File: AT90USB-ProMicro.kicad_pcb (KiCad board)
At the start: 2 copper layers, 18 x 33 mm, 21 parts, among them J1 Conn_01x12, J2 Conn_01x12, J3 Conn_01x03, U1 AT90USB162-16MU, U2 MCP1703A-3302_SOT23, X1 O925208MEDA4SI

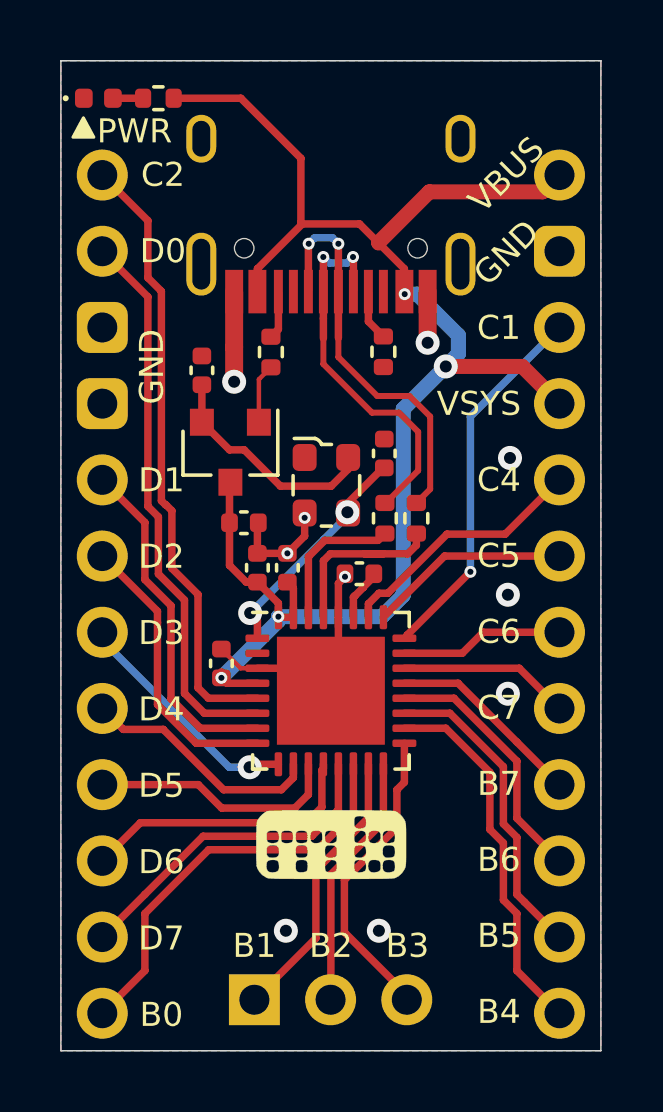
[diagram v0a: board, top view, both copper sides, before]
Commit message: changed oscillator for crystal, 3225 gnd on 2 and 4.
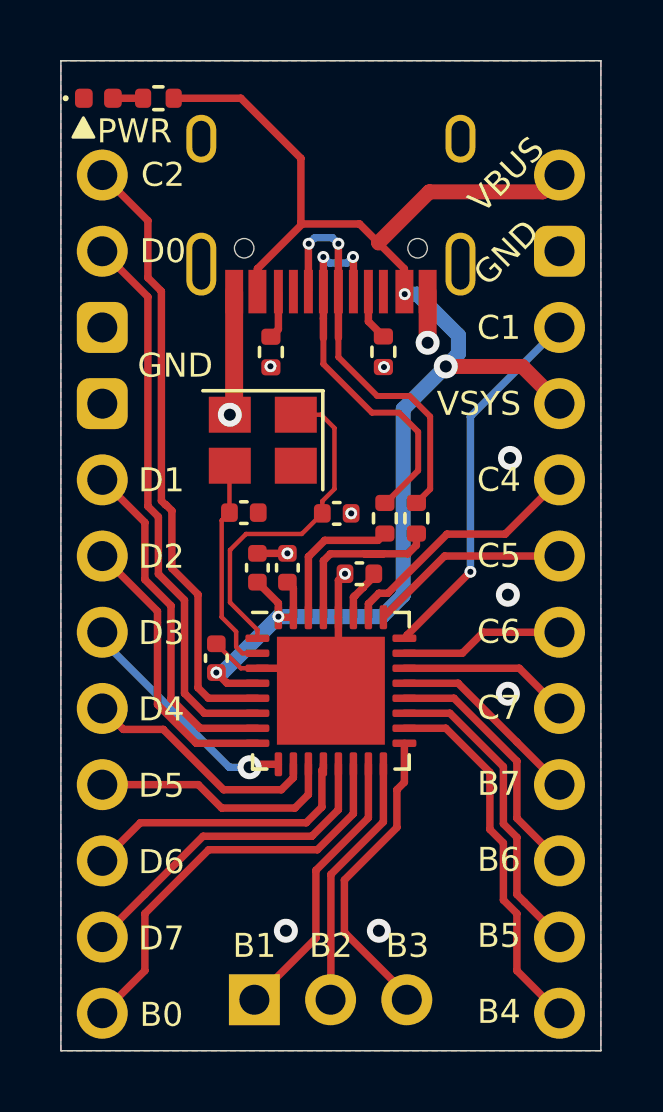
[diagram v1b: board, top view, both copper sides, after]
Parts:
- removed C7: 15pF 0402, Capacitor_SMD:C_0402_1005Metric
- removed Ref**: Val**, MechboardsLogo:mechboardsLOGO_5mm
- removed U2: MCP1703A-3302_SOT23, Package_TO_SOT_SMD:SOT-23
- removed X1: O925208MEDA4SI, Oscillator:Oscillator_SMD_ECS_2520MV-xxx-xx-4Pin_2.5x2.0mm
- added Y1: 8MHz, Crystal:Crystal_SMD_3225-4Pin_3.2x2.5mm, F.Cu at (129.7, 73.6)
- C1, C6: value 0.1uf 0402 -> 0402 22pf
- moved C6 4.94 mm to (129.1, 76.1), turned to 180 degrees
- moved C1 3.11 mm to (132.2, 76.1), turned to 180 degrees
- moved C5 0.24 mm to (128.2, 80.9)
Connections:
- C1 pad 1: VBUS -> GND
- C1 pad 2: GND -> XTAL1
- C6 pad 2: Net-(C6-Pad2) -> XTAL2
- U1 pad 2: (no net) -> XTAL2
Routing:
- net Net-(C6-Pad2): track 7.78 -> 0.00 mm
- net XTAL2: track 0.00 -> 7.25 mm
- net VBUS: track 54.2 -> 50.2 mm
- net XTAL1: track 7.66 -> 11.4 mm, vias 2 -> 0
- net GND: track 18.5 -> 15.4 mm, vias 10 -> 12

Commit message: Added a Kiwi pattern on both sides of the board to make it look "Pretty"
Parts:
- added G***: LOGO, Graphic:tilepattern, F.Cu at (132.0, 77.5)
- added G***: LOGO, Graphic:tilepattern, B.Cu at (132.0, 77.5)
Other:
- board text removed: "PWR"

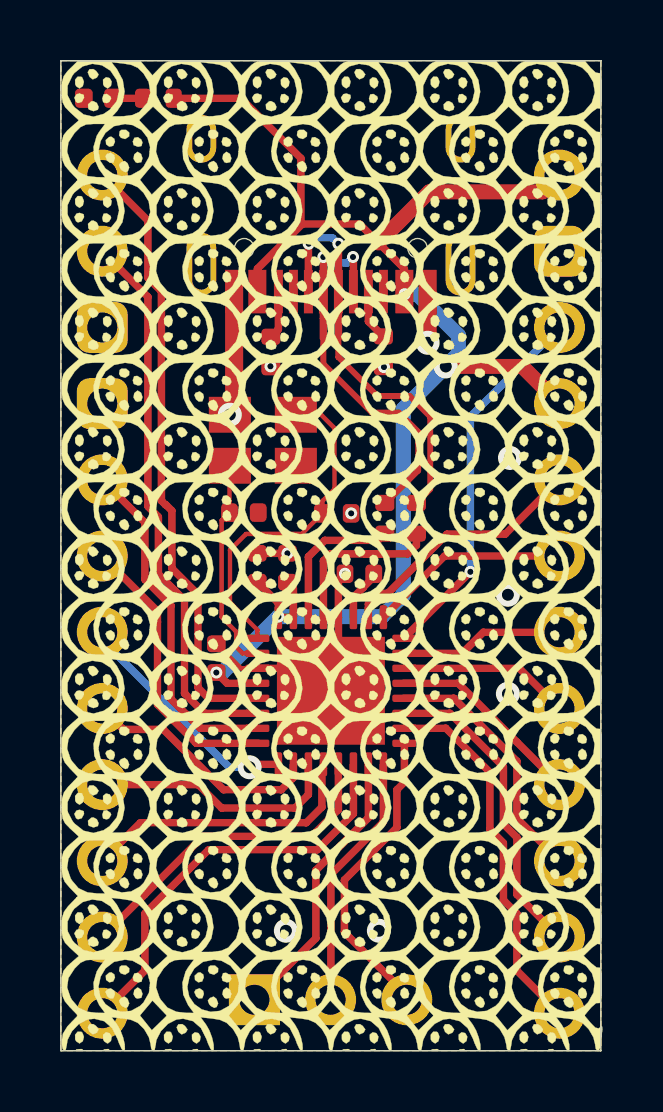
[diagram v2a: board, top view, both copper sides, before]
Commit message: Changed pattern out for a geo graphic looking one, much nicer i think.
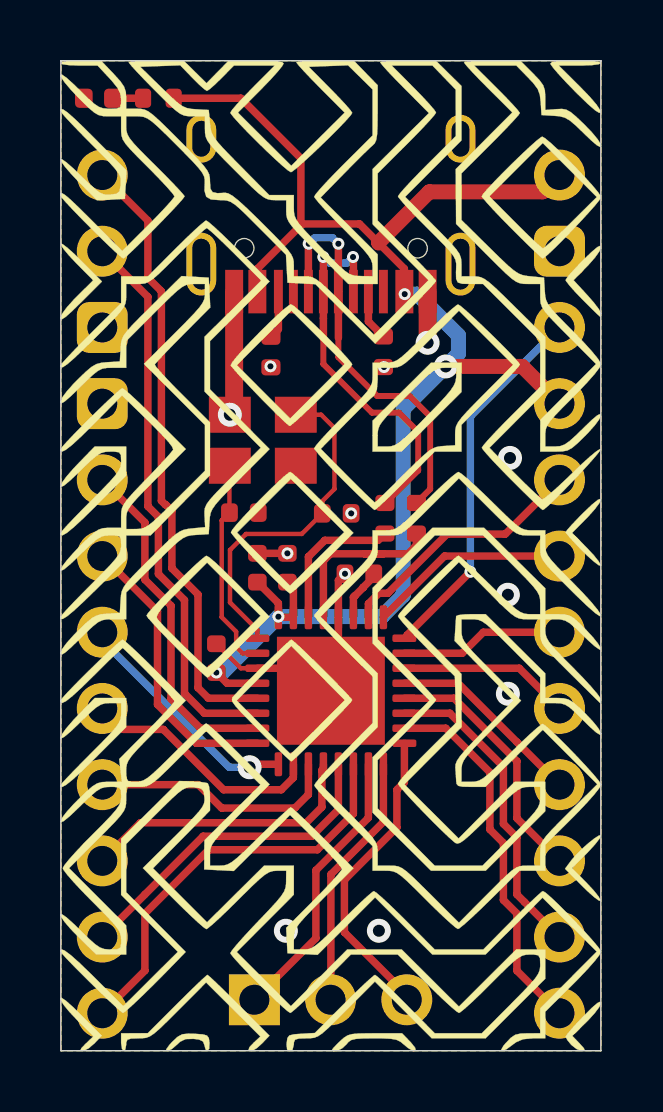
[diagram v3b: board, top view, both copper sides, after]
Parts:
- removed the G*** at (132.0, 77.5) (x2)
- added G***: LOGO, Graphic:Geopattern, B.Cu at (131.9, 77.5)
- added G***: LOGO, Graphic:Geopattern, F.Cu at (131.9, 77.5)
